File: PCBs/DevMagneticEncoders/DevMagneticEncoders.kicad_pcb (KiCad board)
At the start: 2 copper layers, 55 x 56 mm, 23 parts, among them J1 Conn_01x06_Male, J2 Conn_01x06_Male, J3 Screw_Terminal_01x02, J4 Conn_02x03_Odd_Even, J5 Conn_02x03_Odd_Even, J6 Conn_01x06_Male, J7 Conn_01x04_Male, J8 Conn_01x04_Male, U1 AZ1117-3.3, U2 ESP32-S2-WROOM

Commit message: ordered boards
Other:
- board text added: "SAGE ROBOTS A4 DEV BOARD A"

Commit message: 5 stepper board
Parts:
- added A3: Pololu_Breakout_DRV8825, Module:Pololu_Breakout-16_15.2x20.3mm, F.Cu at (92.0, 95.2)
- added A4: Pololu_Breakout_DRV8825, Module:Pololu_Breakout-16_15.2x20.3mm, F.Cu at (110.5, 95.2)
- added A5: Pololu_Breakout_DRV8825, Module:Pololu_Breakout-16_15.2x20.3mm, F.Cu at (129.5, 95.2)
- added C10: 0.1U, Capacitor_SMD:C_0805_2012Metric_Pad1.18x1.45mm_HandSolder, F.Cu at (137.0, 63.0)
- added C11: 100U, Capacitor_SMD:CP_Elec_6.3x7.7, F.Cu at (138.7, 67.5)
- added C12: 100u, Capacitor_SMD:CP_Elec_6.3x7.7, F.Cu at (98.5, 108.8)
- added C13: 100u, Capacitor_SMD:CP_Elec_6.3x7.7, F.Cu at (117.0, 108.8)
- added C14: 100u, Capacitor_SMD:CP_Elec_6.3x7.7, F.Cu at (136.0, 108.8)
- added C15: 0.1u, Capacitor_SMD:C_0805_2012Metric_Pad1.18x1.45mm_HandSolder, F.Cu at (101.5, 113.5)
- added C16: 0.1u, Capacitor_SMD:C_0805_2012Metric_Pad1.18x1.45mm_HandSolder, F.Cu at (120.0, 113.5)
- added C17: 0.1u, Capacitor_SMD:C_0805_2012Metric_Pad1.18x1.45mm_HandSolder, F.Cu at (139.0, 113.5)
- added C7: 0.1u, Capacitor_SMD:C_0805_2012Metric_Pad1.18x1.45mm_HandSolder, F.Cu at (83.0, 113.5)
- added C8: 0.1u, Capacitor_SMD:C_0805_2012Metric_Pad1.18x1.45mm_HandSolder, F.Cu at (83.0, 90.0)
- added C9: 1U, Capacitor_SMD:C_0805_2012Metric_Pad1.18x1.45mm_HandSolder, F.Cu at (134.5, 84.0)
- added J10: Conn_01x06_Male, Connector_JST:JST_XH_B6B-XH-A_1x06_P2.50mm_Vertical, F.Cu at (130.0, 76.0)
- added J11: Conn_01x06_Male, Connector_JST:JST_XH_B6B-XH-A_1x06_P2.50mm_Vertical, F.Cu at (130.0, 83.0)
- added J12: Conn_01x06_Male, Connector_JST:JST_XH_B6B-XH-A_1x06_P2.50mm_Vertical, F.Cu at (130.0, 90.0)
- added J13: Conn_02x03_Odd_Even, Connector_PinHeader_2.54mm:PinHeader_2x03_P2.54mm_Vertical, F.Cu at (98.5, 96.5)
- added J14: Conn_02x03_Odd_Even, Connector_PinHeader_2.54mm:PinHeader_2x03_P2.54mm_Vertical, F.Cu at (117.0, 96.5)
- added J15: Conn_02x03_Odd_Even, Connector_PinHeader_2.54mm:PinHeader_2x03_P2.54mm_Vertical, F.Cu at (136.0, 96.5)
- added J16: Conn_01x04_Male, Connector_JST:JST_XH_B4B-XH-A_1x04_P2.50mm_Vertical, F.Cu at (95.0, 118.5)
- added J17: Conn_01x04_Male, Connector_JST:JST_XH_B4B-XH-A_1x04_P2.50mm_Vertical, F.Cu at (110.0, 118.5)
- added J18: Conn_01x04_Male, Connector_JST:JST_XH_B4B-XH-A_1x04_P2.50mm_Vertical, F.Cu at (125.5, 118.5)
- added J9: Conn_01x02_Male, Connector_JST:JST_XH_B2B-XH-A_1x02_P2.50mm_Vertical, F.Cu at (140.5, 90.0)
- added R5: 0.1, Resistor_SMD:R_0805_2012Metric_Pad1.20x1.40mm_HandSolder, F.Cu at (141.5, 63.0)
- added S2: TL3315NF160Q, A4:TL3305AF160QG, F.Cu at (128.5, 55.0)
- added U3: ZXBM5210-S, Package_SO:SOIC-8_3.9x4.9mm_P1.27mm, F.Cu at (139.5, 82.0)
- added U4: TB67H451FNG,EL, Package_SO:SOIC-8-1EP_3.9x4.9mm_P1.27mm_EP2.29x3mm_ThermalVias, F.Cu at (137.2, 74.5)
- J6: value Conn_01x06_Male -> Conn_01x03_Male; footprint Connector_JST:JST_PH_B6B-PH-K_1x06_P2.00mm_Vertical -> Connector_PinHeader_2.54mm:PinHeader_1x03_P2.54mm_Vertical
- S1: footprint A4:CK_PTS647_4.5x4.5 -> A4:TL3305AF160QG
- moved J1 36.7 mm to (130.0, 62.0), turned to 180 degrees
- moved J2 36.4 mm to (130.0, 69.0), turned to 180 degrees
- moved S1 32.8 mm to (119.0, 55.0)
- moved R1 13.1 mm to (83.0, 92.5), turned to 0 degrees
- moved A1 11.8 mm to (73.5, 95.2), turned to 0 degrees
- moved R2 11.5 mm to (87.0, 92.5), turned to 0 degrees
- moved C3 11.2 mm to (80.0, 108.8), turned to 90 degrees
- moved J4 5.69 mm to (80.0, 96.4), turned to 0 degrees
- moved J5 3.08 mm to (80.0, 72.9)
- moved C4 2.35 mm to (79.5, 85.2)
- moved J6 2.24 mm to (110.5, 72.0), turned to 0 degrees
- moved R4 1.50 mm to (99.0, 92.5), turned to 180 degrees
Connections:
- J6 pad 1: GND -> TX
- J6 pad 2: IO0 -> RX
- J6 pad 3: EN -> GND
- U2 pad 11: Net-(U2-Pad11) -> EN3
- U2 pad 12: Net-(U2-Pad12) -> DIR2
- U2 pad 13: Net-(U2-Pad13) -> STEP2
- U2 pad 14: Net-(U2-Pad14) -> EN2
- U2 pad 15: Net-(U2-Pad15) -> EN1
- U2 pad 16: Net-(U2-Pad16) -> CHARGE
- U2 pad 20: CHARGE -> DAC1
- U2 pad 22: MOSI -> STEP3
- U2 pad 23: CS1 -> DIR3
- U2 pad 24: MISO -> EN4
- U2 pad 25: CLK -> STEP4
- U2 pad 27: CS0 -> DIR4
- U2 pad 28: Net-(U2-Pad28) -> CS4
- U2 pad 29: Net-(U2-Pad29) -> CLK
- U2 pad 30: Net-(U2-Pad30) -> CS3
- U2 pad 31: Net-(U2-Pad31) -> MOSI
- U2 pad 32: Net-(U2-Pad32) -> MOT1
- U2 pad 33: Net-(U2-Pad33) -> MOT2
- U2 pad 34: Net-(U2-Pad34) -> MISO
- U2 pad 35: Net-(U2-Pad35) -> CS2
- U2 pad 36: Net-(U2-Pad36) -> CS1
- U2 pad 39: Net-(U2-Pad39) -> CS0
- U2 pad 6: EN1 -> Net-(U2-Pad6)
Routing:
- net +12V: track 111.9 -> 220.1 mm
- net GND: track 121.7 -> 192.8 mm
- net DAC1: track 0.00 -> 66.4 mm, vias 0 -> 2
- net EN4: track 0.00 -> 59.9 mm
- net EN3: track 0.00 -> 53.6 mm, vias 0 -> 1
- net MOT2: track 0.00 -> 46.5 mm, vias 0 -> 2
- net STEP4: track 0.00 -> 43.0 mm
- net MOT1: track 0.00 -> 41.3 mm, vias 0 -> 2
- net DIR4: track 0.00 -> 37.8 mm
- net EN2: track 0.00 -> 35.6 mm, vias 0 -> 1
- net STEP3: track 0.00 -> 28.7 mm
- net CLK: track 19.4 -> 46.8 mm
- net DIR3: track 0.00 -> 25.6 mm
- net OUT1: track 0.00 -> 24.6 mm, vias 0 -> 2
- net STEP2: track 0.00 -> 23.3 mm, vias 0 -> 1
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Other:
- board size 55 x 56 mm -> 83 x 71 mm
- board text removed: "MOSI"

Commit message: ready to order
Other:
- board text added: "+"
- board text added: "0"
- board text added: "1"
- board text added: "12V"
- board text added: "2"
- board text added: "3"
- board text added: "4"
- board text added: "EN"
- board text added: "G"
- board text added: "GND"
- board text added: "IO0"
- board text added: "RX"
- board text added: "SAGE ROBOTS A4 2.0"
- board text removed: "SAGE ROBOTS A4 DEV BOARD A"

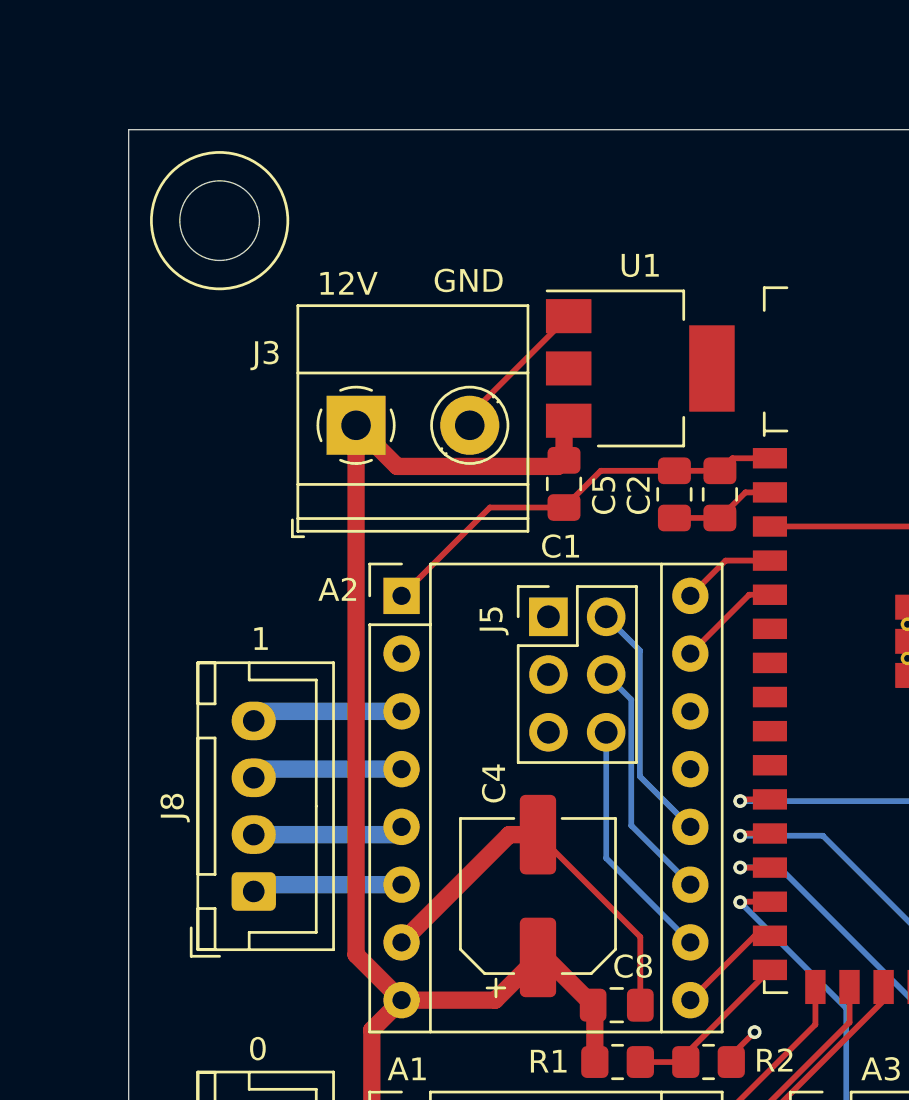
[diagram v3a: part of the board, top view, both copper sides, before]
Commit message: added load cell connector
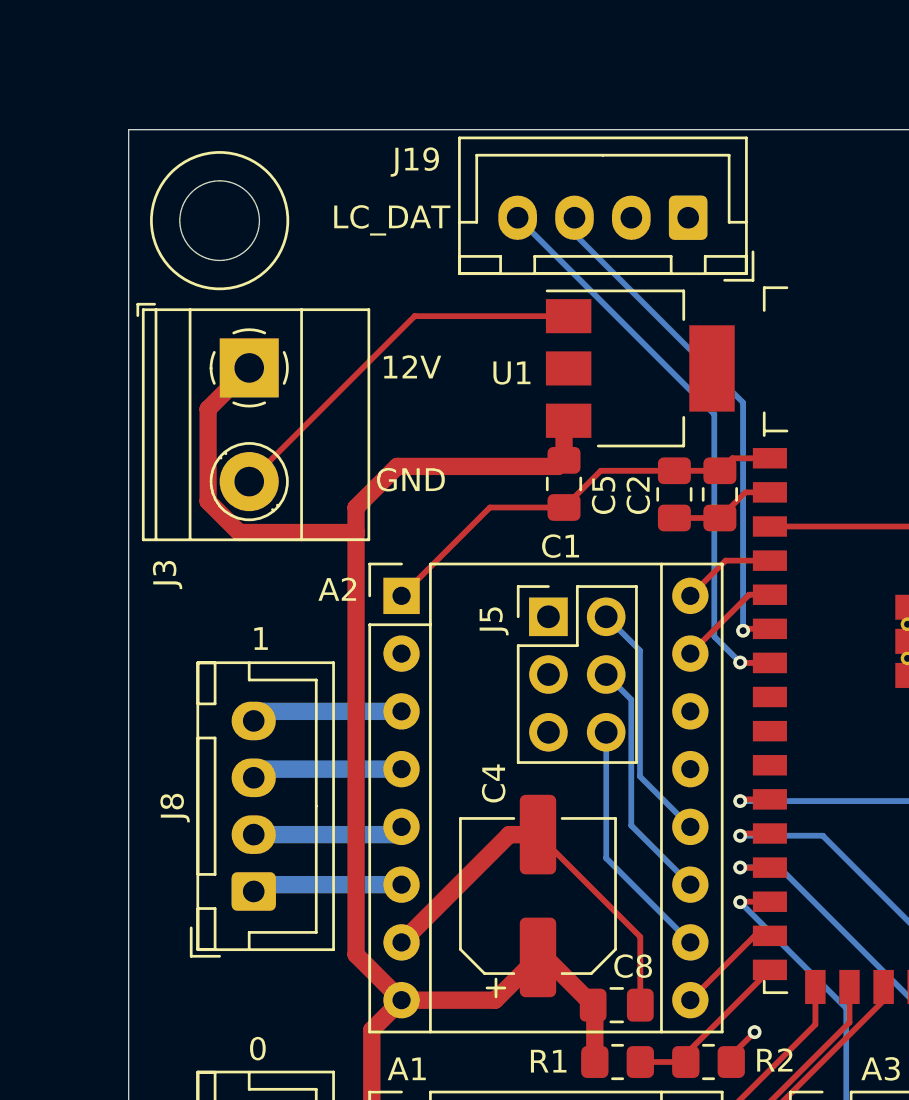
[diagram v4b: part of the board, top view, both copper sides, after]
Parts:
- added J19: Conn_01x04_Male, Connector_JST:JST_XH_B4B-XH-A_1x04_P2.50mm_Vertical, F.Cu at (86.1, 55.4)
- moved J3 5.33 mm to (66.8, 62.0), turned to 270 degrees
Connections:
- U2 pad 6: Net-(U2-Pad6) -> LC_CLK
- U2 pad 7: Net-(U2-Pad7) -> LC_DAT
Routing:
- net LC_DAT: track 0.00 -> 24.9 mm, vias 0 -> 1
- net LC_CLK: track 0.00 -> 22.4 mm, vias 0 -> 1
- net GND: track 192.8 -> 203.2 mm
- net +12V: track 220.1 -> 230.2 mm
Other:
- board text added: "LC_DAT"
